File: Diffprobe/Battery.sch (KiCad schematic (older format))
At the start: 18 parts

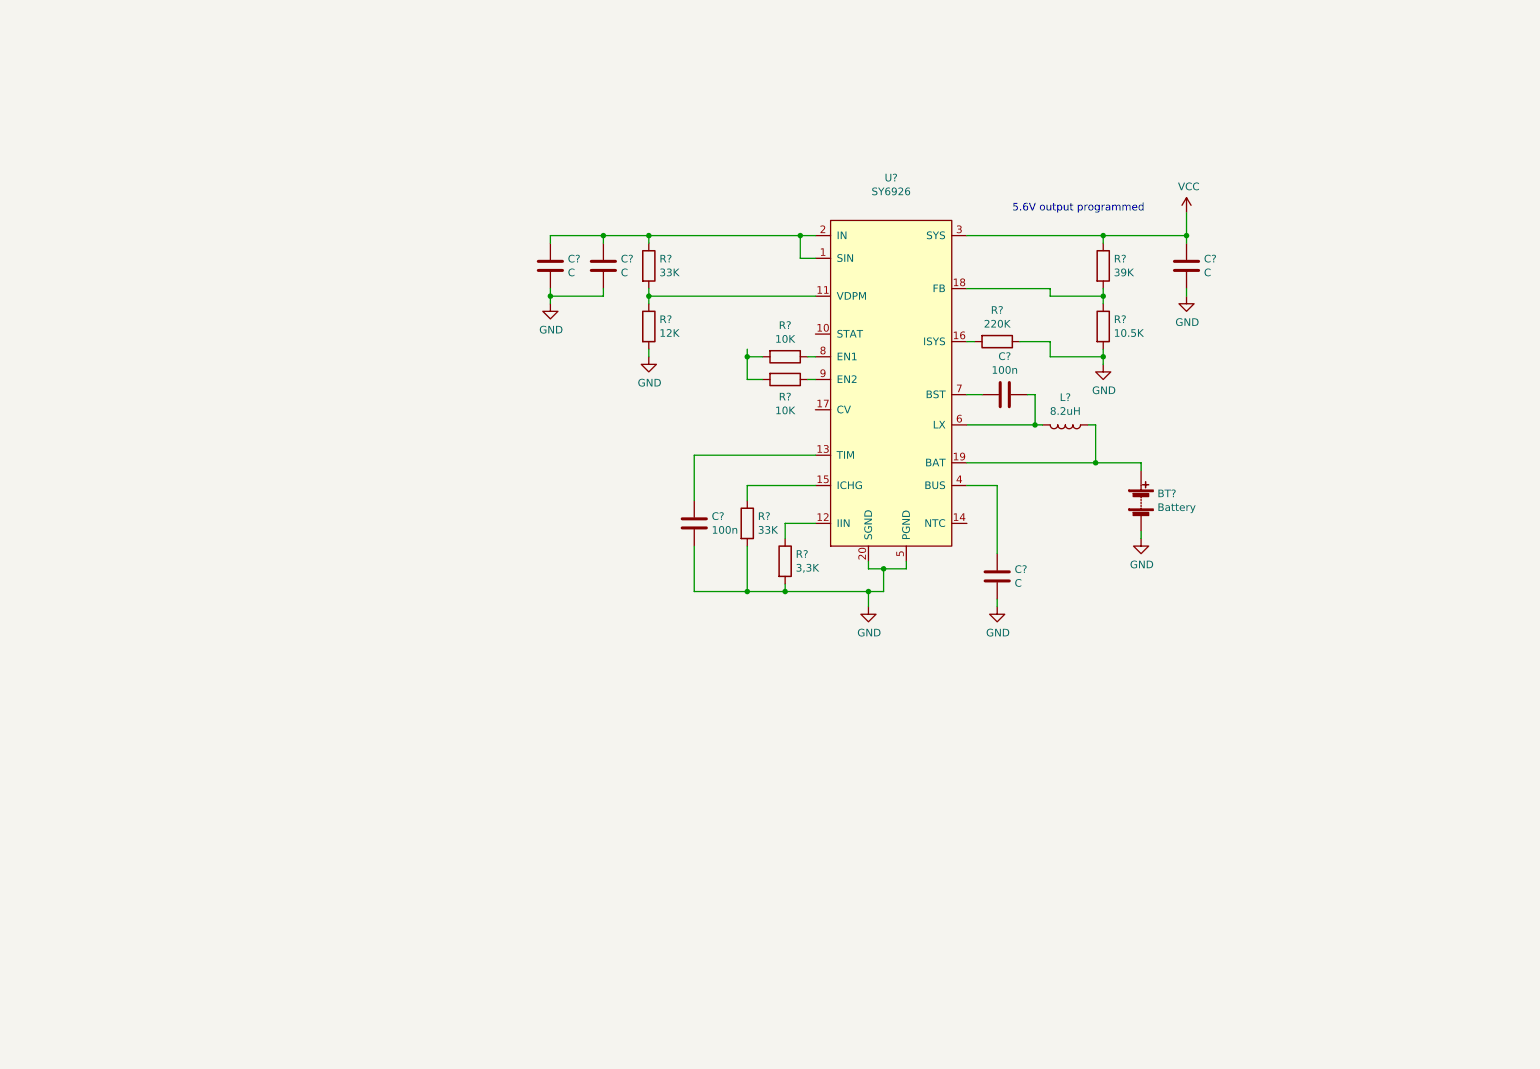
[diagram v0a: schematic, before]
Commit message: more circuitry & simulation added
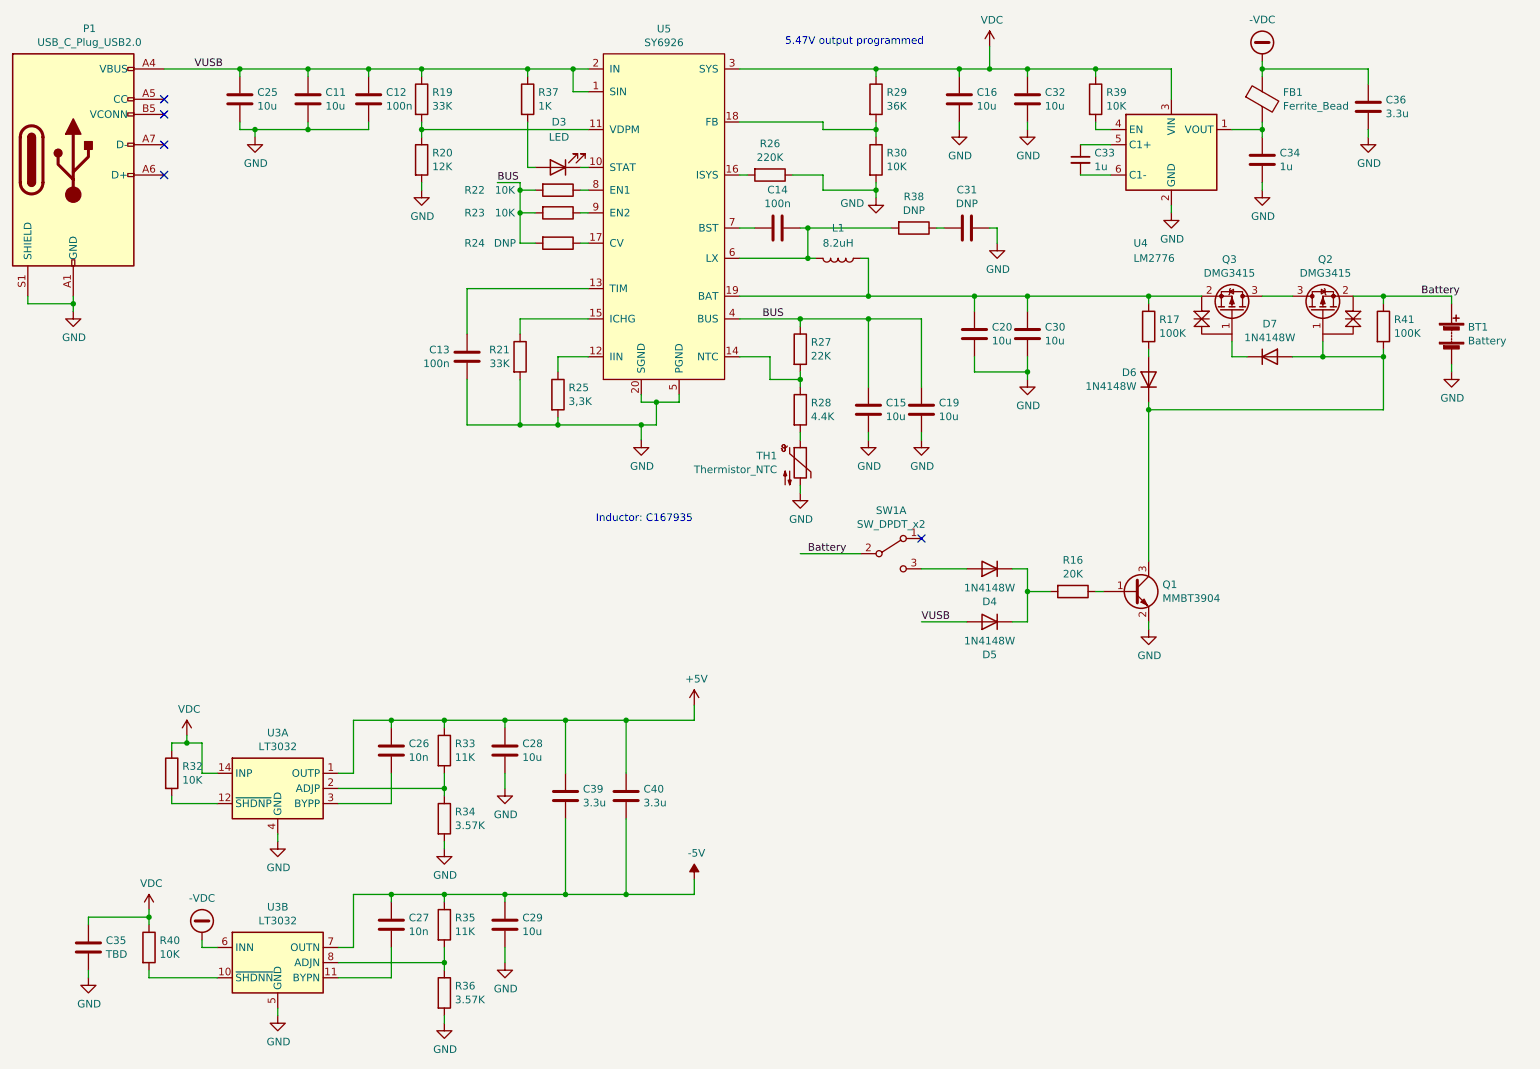
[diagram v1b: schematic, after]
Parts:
- added C19, C20, C25, C28, C29, C30, C32: 10u, Capacitor_SMD:C_0805_2012Metric, symbol Device:C
- added C26, C27: 10n, Capacitor_SMD:C_0805_2012Metric, symbol Device:C
- added C31: DNP, Capacitor_SMD:C_0805_2012Metric, symbol Device:C
- added C33: 1u, Capacitor_SMD:C_0805_2012Metric, symbol Device:C_Small
- added C34: 1u, Capacitor_SMD:C_0805_2012Metric, symbol Device:C
- added C35: TBD, Capacitor_SMD:C_0805_2012Metric, symbol Device:C
- added C36, C39, C40: 3.3u, Capacitor_SMD:C_0805_2012Metric, symbol Device:C
- added D3: LED, LED_SMD:LED_0805_2012Metric, symbol Device:LED
- added D4, D5, D6, D7: 1N4148W, Diode_SMD:D_SOD-123, symbol Diode:1N4148W
- added FB1: Ferrite_Bead, Inductor_SMD:L_0805_2012Metric, symbol Device:Ferrite_Bead
- added P1: USB_C_Plug_USB2.0, Connector_USB:USB_C_Receptacle_XKB_U262-16XN-4BVC11, symbol Connector:USB_C_Plug_USB2.0
- added Q1: MMBT3904, Package_TO_SOT_SMD:SOT-23, symbol Transistor_BJT:MMBT3904
- added Q2, Q3: DMG3415, symbol custom_comps:DMG3415
- added R16: 20K, symbol Device:R
- added R17, R41: 100K, symbol Device:R
- added R24, R38: DNP, Resistor_SMD:R_0805_2012Metric, symbol Device:R
- added R27: 22K, Resistor_SMD:R_0805_2012Metric, symbol Device:R
- added R28: 4.4K, Resistor_SMD:R_0805_2012Metric, symbol Device:R
- added R32, R39, R40: 10K, Resistor_SMD:R_0603_1608Metric, symbol Device:R
- added R33, R35: 11K, Resistor_SMD:R_0805_2012Metric, symbol Device:R
- added R34, R36: 3.57K, Resistor_SMD:R_0805_2012Metric, symbol Device:R
- added R37: 1K, Resistor_SMD:R_0805_2012Metric, symbol Device:R
- added SW1: SW_DPDT_x2, symbol Switch:SW_DPDT_x2
- added TH1: Thermistor_NTC, TestPoint:TestPoint_2Pads_Pitch2.54mm_Drill0.8mm, symbol Device:Thermistor_NTC
- added U3: LT3032, Package_DFN_QFN:Linear_DE14MA, symbol Regulator_Linear:LT3032
- added U4: LM2776, Package_TO_SOT_SMD:SOT-23-6, symbol Regulator_SwitchedCapacitor:LM2776
- BT1: renamed from BT?; footprint (none) -> TestPoint:TestPoint_2Pads_Pitch2.54mm_Drill0.8mm
- C11, C15, C16: renamed from C?; value C -> 10u; footprint (none) -> Capacitor_SMD:C_0805_2012Metric
- C12: renamed from C?; value C -> 100n; footprint (none) -> Capacitor_SMD:C_0805_2012Metric
- C13, C14: renamed from C?; footprint (none) -> Capacitor_SMD:C_0805_2012Metric
- L1: renamed from L?; footprint (none) -> Inductor_SMD:L_Taiyo-Yuden_MD-5050
- R19, R20, R21, R25, R26: renamed from R?; footprint (none) -> Resistor_SMD:R_0805_2012Metric
- R22, R23: renamed from R?; footprint (none) -> Resistor_SMD:R_0603_1608Metric
- R29: renamed from R?; value 39K -> 36K; footprint (none) -> Resistor_SMD:R_0805_2012Metric
- R30: renamed from R?; value 10.5K -> 10K; footprint (none) -> Resistor_SMD:R_0603_1608Metric
- U5: renamed from U?; footprint (none) -> custom_coms:QFN-20_L4.0-W4.0-P0.45-BL
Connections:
- net GND: now also C19.2, C20.2, C25.2, C28.2, C29.2, C30.2, C31.1, C32.2, C34.2, C35.2, C36.2, P1.A1 (GND), P1.A12 (GND), P1.B1 (GND), P1.B12 (GND), P1.S1 (SHIELD), Q1.2 (E), R34.2, R36.2, TH1.2, U3.4 (GND), U3.5 (GND), U4.2 (GND)
- net VUSB: now reaches C11.1, C12.1, R19.1, U5.1 (SIN), U5.2 (IN)
- net VUSB: now also C25.1, D5.2 (A), P1.A4 (VBUS), P1.A9 (VBUS), P1.B4 (VBUS), P1.B9 (VBUS), R37.1
- net at U5.10 (STAT): now also D3.1 (K)
- net at U5.14 (NTC): now also R27.2, R28.1
- net at U5.17 (CV): now also R24.1
- net at L1.1, U5.19 (BAT): now also C20.1, C30.1, Q3.2, R17.1; no longer BT1.1 (+)
- net BUS: now reaches C15.1, U5.4 (BUS)
- net BUS: now also R22.2, R23.2, C19.1, R24.2, R27.1
- net at C14.1, L1.2, U5.6 (LX): now also R38.2
- net VCC renamed VDC
- net VDC: now also C32.1, C35.1, R32.1, R39.1, R40.1, U3.14 (INP), U4.3 (VIN)
- new net: R28.2, TH1.1
- new net: D3.2 (A), R37.2
- new net: R32.2, U3.12 (~SHDNP)
- new net: R33.2, R34.1, U3.2 (ADJP)
- new net: C26.2, U3.3 (BYPP)
- new net: R40.2, U3.10 (~SHDNN)
- new net: C27.2, U3.11 (BYPN)
- new net: R35.2, R36.1, U3.8 (ADJN)
- new net: C31.2, R38.1
- new net: C33.1, U4.5 (C1+)
- new net: C33.2, U4.6 (C1-)
- new net: C34.1, FB1.2, U4.1 (VOUT)
- new net: R39.2, U4.4 (EN)
- new net: Q1.1 (B), R16.1
- new net: D6.1 (K), D7.2 (A), Q1.3 (C), Q2.1, R41.2
- new net: D7.1 (K), Q3.1
- new net: D6.2 (A), R17.2
- new net: D4.1 (K), D5.1 (K), R16.2
- new net: D4.2 (A), SW1.3 (C)
- new net: Q2.3, Q3.3
- new net +5V: C26.1, C28.1, C39.1, C40.1, R33.1, U3.1 (OUTP)
- new net -5V: C27.1, C29.1, C39.2, C40.2, R35.1, U3.7 (OUTN)
- new net -VDC: C36.1, FB1.1, U3.6 (INN), U3.9 (INN)
- new net Battery: BT1.1 (+), Q2.2, R41.1, SW1.2 (B)
- no-connect marks 0 -> 5
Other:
- note added: "5.47V output programmed\n"
- note added: "Inductor: C167935"
- note removed: "5.6V output programmed\n"
- moved on the sheet: BT1, C11, C12, C13, C14, C15, C16, L1, R19, R20, R21, R22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

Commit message: readme, 3d files, measurements and more added
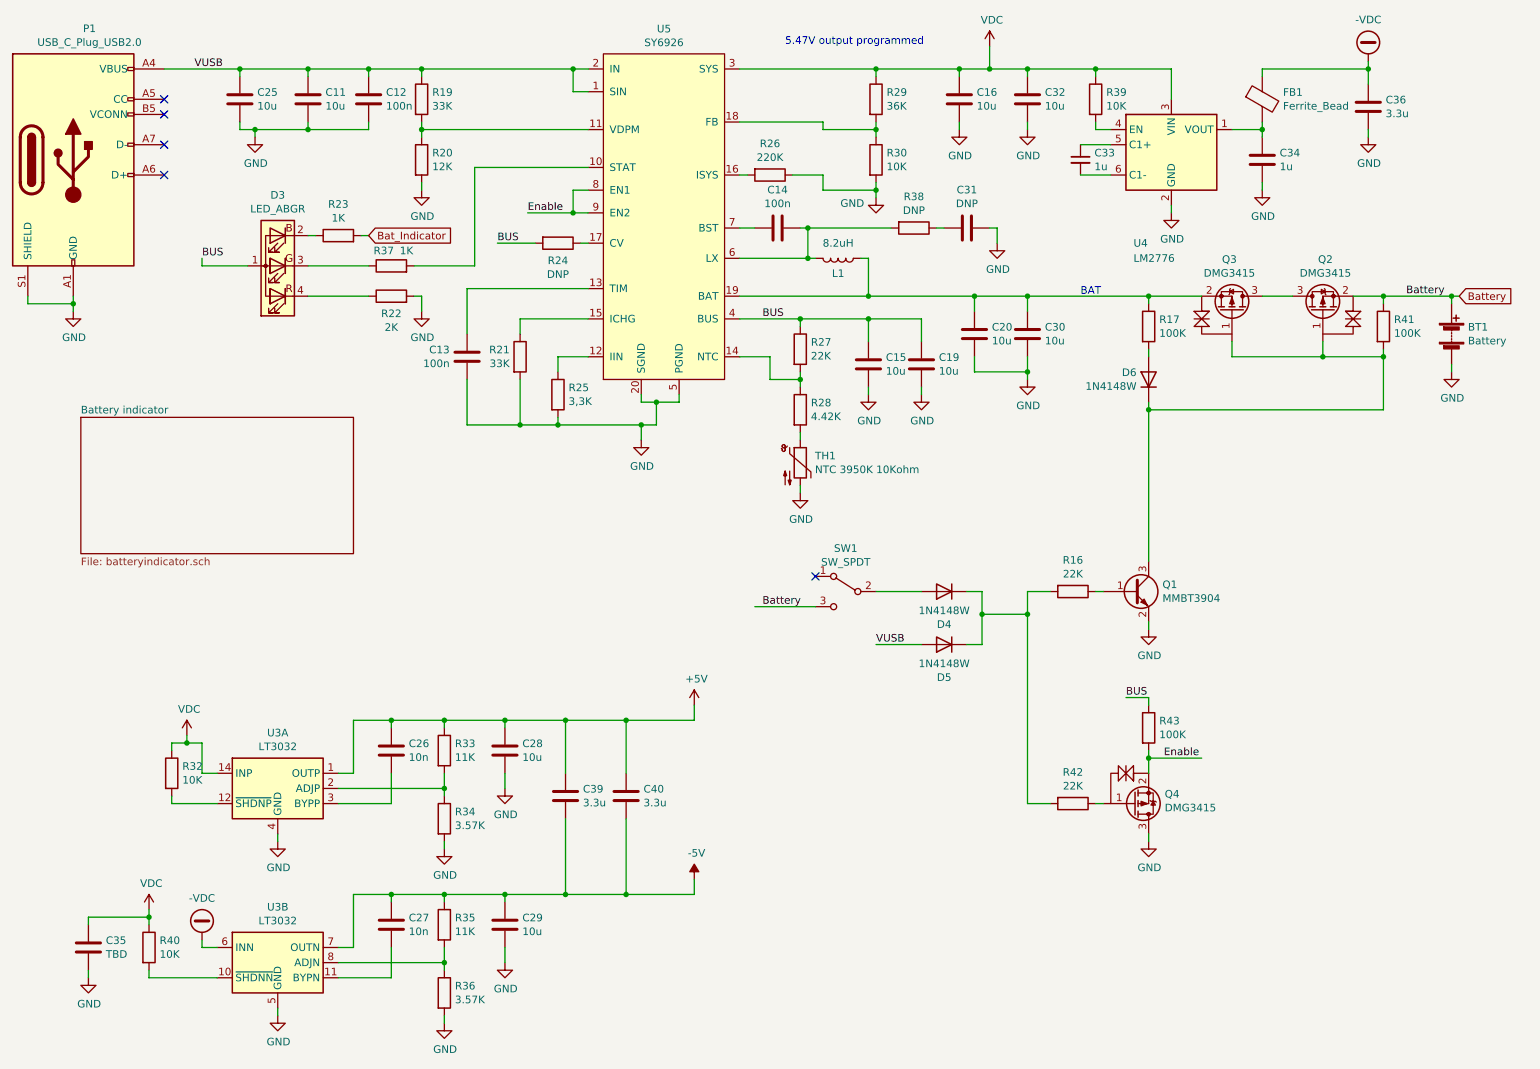
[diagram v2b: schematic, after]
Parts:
- removed D3: LED, LED_SMD:LED_0805_2012Metric, symbol Device:LED
- removed D7: 1N4148W, Diode_SMD:D_SOD-123, symbol Diode:1N4148W
- removed SW1: SW_DPDT_x2, symbol Switch:SW_DPDT_x2
- added D3: LED_ABGR, custom_coms:MHS110_RGB, symbol Device:LED_ABGR
- added Q4: DMG3415, Package_TO_SOT_SMD:SOT-23, symbol custom_comps:DMG3415
- added R42: 22K, Resistor_SMD:R_0805_2012Metric, symbol Device:R
- added R43: 100K, Resistor_SMD:R_0805_2012Metric, symbol Device:R
- added SW1: SW_SPDT, Button_Switch_THT:SW_CuK_OS102011MA1QN1_SPDT_Angled, symbol Switch:SW_SPDT
- BT1: footprint TestPoint:TestPoint_2Pads_Pitch2.54mm_Drill0.8mm -> Connector_JST:JST_XH_B2B-XH-A_1x02_P2.50mm_Vertical
- C11, C15, C16, C19, C20, C25, C28, C29, C30, C32: LCSC (none) -> C15850
- C33, C34: LCSC (none) -> C282733
- C36, C39, C40: LCSC (none) -> C38332
- L1: LCSC (none) -> C167935
- P1: LCSC (none) -> C393939
- Q2, Q3: footprint (none) -> Package_TO_SOT_SMD:SOT-23
- R16: value 20K -> 22K; footprint (none) -> Resistor_SMD:R_0805_2012Metric; LCSC (none) -> C114565
- R17, R41: footprint (none) -> Resistor_SMD:R_0805_2012Metric
- R19, R21: LCSC (none) -> C147826
- R22: value 10K -> 2K; footprint Resistor_SMD:R_0603_1608Metric -> Resistor_SMD:R_0805_2012Metric
- R23: value 10K -> 1K; footprint Resistor_SMD:R_0603_1608Metric -> Resistor_SMD:R_0805_2012Metric
- R27: LCSC (none) -> C114565
- R28: value 4.4K -> 4.42K
- R29: LCSC (none) -> C168444
- R30, R39: footprint Resistor_SMD:R_0603_1608Metric -> Resistor_SMD:R_0805_2012Metric
- R34, R36: LCSC (none) -> C245322
- R37: LCSC (none) -> C880597
- TH1: value Thermistor_NTC -> NTC 3950K 10Kohm; LCSC (none) -> C123378
- U3: LCSC (none) -> C514419
- U4: LCSC (none) -> C69527
- U5: LCSC (none) -> C180877
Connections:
- net BUS: now also D3.1 (A), R43.1; no longer R22.2, R23.2
- net Battery: now also SW1.3 (C)
- net GND: now also R22.2, Q4.3
- net VUSB: no longer R37.1
- net at U5.10 (STAT): now also R37.2
- net at R22.1: now also D3.4 (RK); no longer U5.8 (EN1)
- net at R23.1: now also D3.2 (BK); no longer U5.9 (EN2)
- net at D6.1 (K), Q1.3 (C), Q2.1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: now also Q3.1
- net at D4.1 (K), D5.1 (K), R16.2: now also R42.2
- net at D4.2 (A): now also SW1.2 (B)
- new net: D3.3 (GK), R37.1
- new net: Q4.1, R42.1
- new net Bat_Indicator: R23.2
- new net Enable: Q4.2, R43.2, U5.8 (EN1), U5.9 (EN2)
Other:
- note added: "BAT"
- note removed: "Inductor: C167935"
- moved on the sheet: C15, C19, D4, D5, R37
